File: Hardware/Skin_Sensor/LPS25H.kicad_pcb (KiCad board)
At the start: 2 copper layers, 55 x 55 mm, 49 parts, among them SW1 SW_PUSH, U1 ADP7102, U2 ATSAMD21E18A, U3 AVRISP, U4 LSM9DS1, U5 LP5521YQ, X1 ABS06

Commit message: Fixed pour issues
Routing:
- net GND: track 196.5 -> 200.9 mm, vias 12 -> 11
- net (no net): track 0.32 -> 0.37 mm, vias 0 -> 1
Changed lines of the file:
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@@
     (links 162)
     (no_connects 0)
-    (area 130.545445 70.825409 205.880001 129.245302)
+    (area 123.2 69.2 205.880001 130.350001)
     (thickness 1.6)
     (drawings 91)
@@
   (segment (start 159.172703 87.557501) (end 159.172703 87.840344) (width 0.25) (layer B.Cu) (net 0))
   (segment (start 159.137348 88.47674) (end 159.137348 88.512095) (width 0.25) (layer B.Cu) (net 0))
-  (segment (start 158.9984 104.9484) (end 159 104.95) (width 0.25) (layer F.Cu) (net 0))
+  (segment (start 153.05 102.5) (end 153.05 102.45) (width 0.2) (layer F.Cu) (net 0))
+  (via (at 153.05 102.45) (size 0.6) (drill 0.4) (layers F.Cu B.Cu) (net 0))
   (segment (start 165.75 103) (end 164.55 104.2) (width 0.5) (layer B.Cu) (net 1))
   (via (at 165.3 94.65) (size 0.6) (drill 0.4) (layers F.Cu B.Cu) (net 1))
@@
   (segment (start 158.394885 81.053514) (end 158.394885 85.05) (width 0.25) (layer F.Cu) (net 1))
   (segment (start 158.394885 85.05) (end 158.394885 85.082627) (width 0.25) (layer F.Cu) (net 1))
-  (segment (start 163.6 107.55) (end 163.55 107.6) (width 0.25) (layer B.Cu) (net 2))
+  (segment (start 160 109.15) (end 162.7 109.15) (width 0.25) (layer B.Cu) (net 2))
   (via (at 163.5 107.6) (size 0.6) (drill 0.4) (layers F.Cu B.Cu) (net 2))
-  (segment (start 163.55 107.6) (end 163.5 107.6) (width 0.25) (layer B.Cu) (net 2))
-  (segment (start 164.9 102.15) (end 165 102.05) (width 0.25) (layer F.Cu) (net 2) (status C00000))
-  (segment (start 165 102.05) (end 165 100.7) (width 0.25) (layer F.Cu) (net 2) (status 400000))
+  (segment (start 163.5 108.35) (end 163.5 107.6) (width 0.25) (layer B.Cu) (net 2))
+  (segment (start 162.7 109.15) (end 163.5 108.35) (width 0.25) (layer B.Cu) (net 2))
+  (segment (start 164.9 102.15) (end 165 102.05) (width 0.25) (layer F.Cu) (net 2))
+  (segment (start 165 102.05) (end 165 100.7) (width 0.25) (layer F.Cu) (net 2))
   (via (at 165 100.7) (size 0.6) (drill 0.4) (layers F.Cu B.Cu) (net 2))
-  (segment (start 165.4 101.425) (end 164.9 101.925) (width 0.25) (layer F.Cu) (net 2) (status C00000))
-  (segment (start 164.9 101.925) (end 164.9 102.15) (width 0.25) (layer F.Cu) (net 2) (status C00000))
+  (segment (start 165.4 101.425) (end 164.9 101.925) (width 0.25) (layer F.Cu) (net 2))
+  (segment (start 164.9 101.925) (end 164.9 102.15) (width 0.25) (layer F.Cu) (net 2))
   (segment (start 164.175 104.375) (end 164.075 104.375) (width 0.25) (layer F.Cu) (net 2))
   (via (at 163 103.2) (size 0.6) (drill 0.4) (layers F.Cu B.Cu) (net 2))
   (segment (start 163 103.3) (end 163 103.2) (width 0.25) (layer F.Cu) (net 2))
   (segment (start 164.075 104.375) (end 163 103.3) (width 0.25) (layer F.Cu) (net 2))
-  (via (at 159.4 100.65) (size 0.6) (drill 0.4) (layers F.Cu B.Cu) (net 2) (status 800000))
-  (segment (start 159.4 100.65) (end 160 100.05) (width 0.2) (layer F.Cu) (net 2) (status C00000))
-  (segment (start 160 100.05) (end 160 100) (width 0.2) (layer F.Cu) (net 2) (status C00000))
-  (segment (start 153.05 102.5) (end 153.05 102.45) (width 0.2) (layer F.Cu) (net 2))
-  (via (at 153.05 102.45) (size 0.6) (drill 0.4) (layers F.Cu B.Cu) (net 2))
+  (via (at 159.4 100.65) (size 0.6) (drill 0.4) (layers F.Cu B.Cu) (net 2))
+  (segment (start 159.4 100.65) (end 160 100.05) (width 0.2) (layer F.Cu) (net 2))
+  (segment (start 160 100.05) (end 160 100) (width 0.2) (layer F.Cu) (net 2))
   (segment (start 162.04 109.25) (end 160.1 109.25) (width 0.2) (layer F.Cu) (net 2))
   (via (at 160 109.15) (size 0.6) (drill 0.4) (layers F.Cu B.Cu) (net 2))
@@
   (segment (start 162.8 102.55) (end 163.25 102.55) (width 0.25) (layer F.Cu) (net 3))
   (segment (start 163.25 102.55) (end 163.65 102.95) (width 0.25) (layer F.Cu) (net 3))
-  (segment (start 162.35 103.6) (end 162 103.95) (width 0.25) (layer F.Cu) (net 3) (status 800000))
+  (segment (start 162.35 103.6) (end 162 103.95) (width 0.25) (layer F.Cu) (net 3))
   (segment (start 163.65 103.35) (end 163.65 102.95) (width 0.25) (layer F.Cu) (net 3))
   (segment (start 164.2 103.9) (end 163.65 103.35) (width 0.25) (layer F.Cu) (net 3))
   (segment (start 163.4 106.7) (end 163.4 104.3) (width 0.25) (layer F.Cu) (net 3))
   (segment (start 163.4 104.3) (end 163.05 103.95) (width 0.25) (layer F.Cu) (net 3))
-  (segment (start 163.05 103.95) (end 162 103.95) (width 0.25) (layer F.Cu) (net 3) (status 800000))
+  (segment (start 163.05 103.95) (end 162 103.95) (width 0.25) (layer F.Cu) (net 3))
   (segment (start 162.9 107.4) (end 162.9 107.95) (width 0.25) (layer F.Cu) (net 3))
   (segment (start 163.4 106.7) (end 162.9 107.2) (width 0.25) (layer F.Cu) (net 3))
@@
   (via (at 164.1 102.5) (size 0.6) (drill 0.4) (layers F.Cu B.Cu) (net 41))
   (segment (start 166 101.7) (end 165.2 102.5) (width 0.2) (layer B.Cu) (net 41))
-  (segment (start 164.25 103.25) (end 164.9 103.25) (width 0.25) (layer F.Cu) (net 41) (status 800000))
+  (segment (start 164.25 103.25) (end 164.9 103.25) (width 0.25) (layer F.Cu) (net 41))
   (segment (start 164.1 103.1) (end 164.25 103.25) (width 0.25) (layer F.Cu) (net 41))
   (segment (start 168.215 98.725) (end 168.215 99) (width 0.2) (layer F.Cu) (net 41))

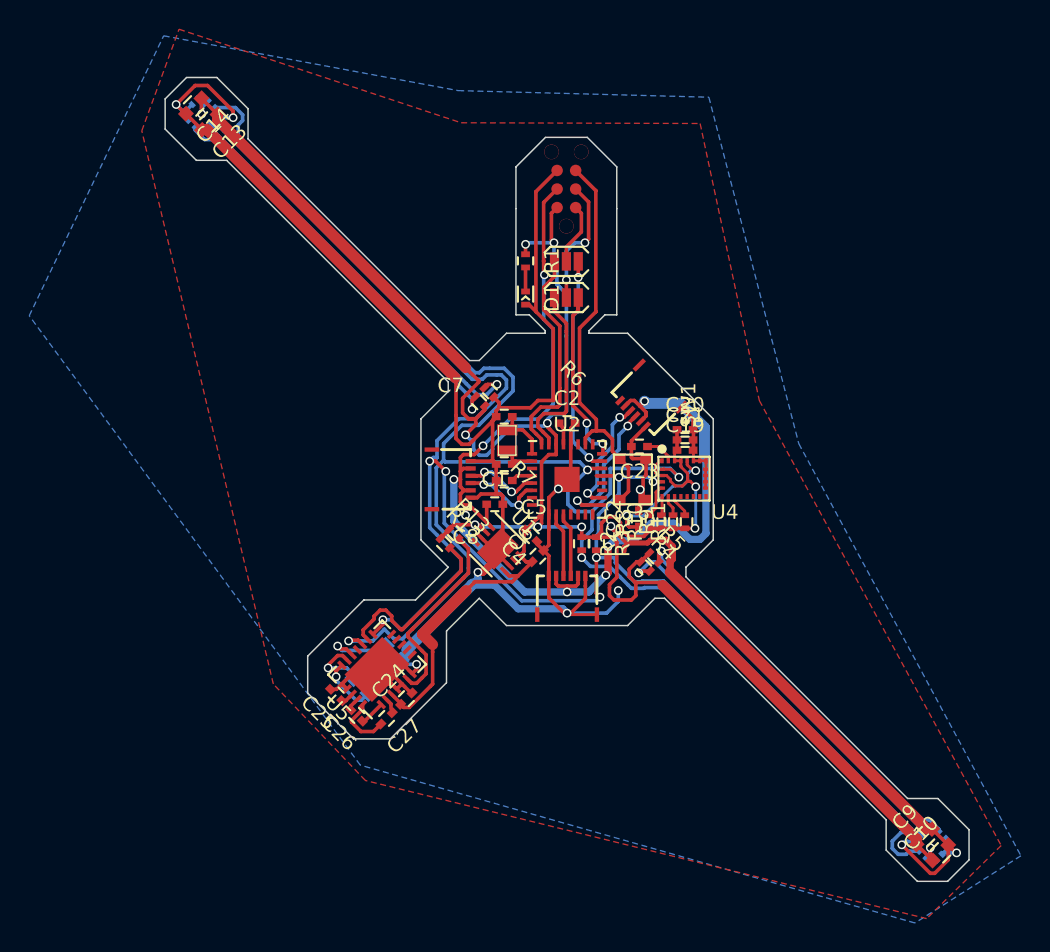
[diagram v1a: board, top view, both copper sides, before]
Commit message: Added sensor and cleaned up the board
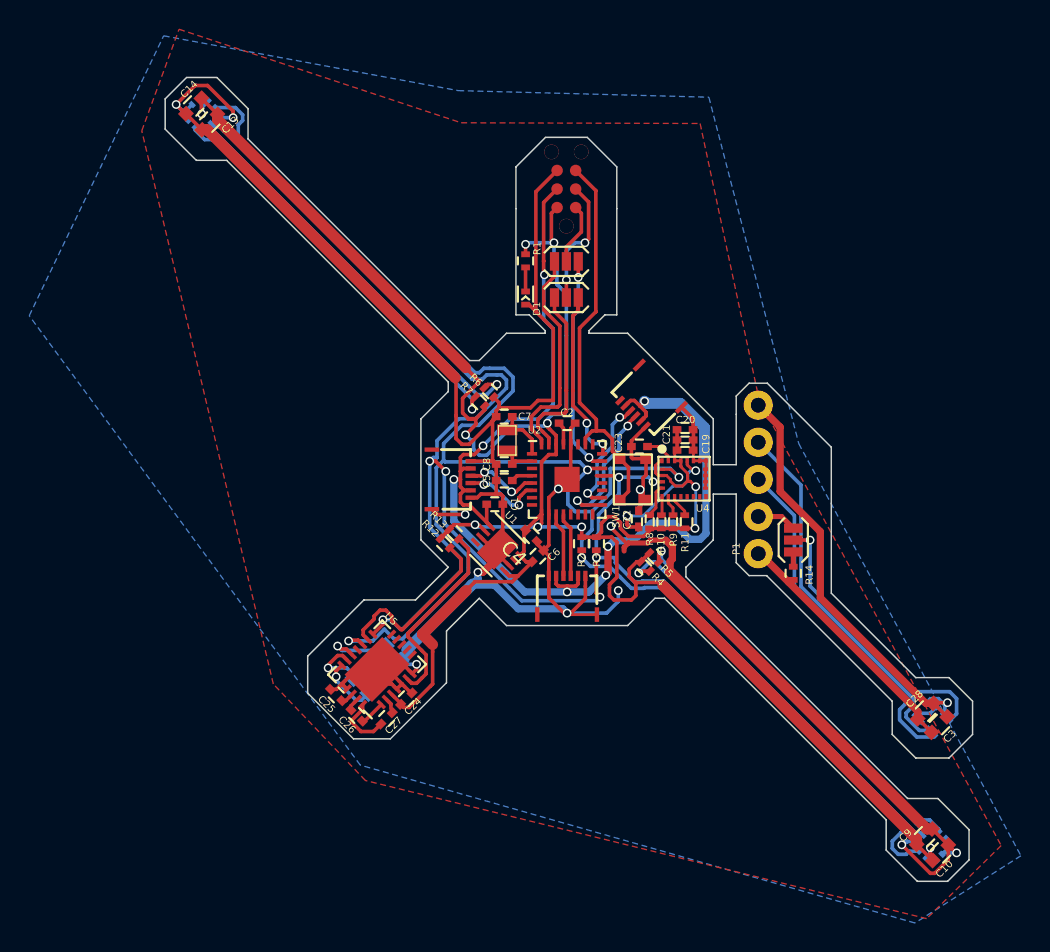
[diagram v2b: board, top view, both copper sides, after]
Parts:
- added C15: sj2, _Fab_Footprint:SJ-2-1-no, F.Cu at (175.5, 104.2)
- added C28: 100nF, Capacitors_SMD:C_0603, F.Cu at (184.5, 115.8)
- added C3: 100nF, Capacitors_SMD:C_0603, F.Cu at (185.5, 116.8)
- added P1: CONN_01X05, _Fab_Footprint:2.54mmX05, F.Cu at (173.1, 100.0)
- added R14: 100k, Resistors_SMD:R_0402, F.Cu at (175.5, 106.4)
- added U6: DPS310, _CSL:8-LGA, B.Cu at (185.0, 116.3)
- C19: value 100nF -> 10uF
- C22: value 100nF -> 10nF
- C24, C25: value 4.7UF -> 1uF
- C26, C27: value 4.7UF -> 0.47uF
- R1: value 10k -> 330
- R10, R11, R12, R13, R4, R5, R6, R7, R8, R9: value RES -> 10k
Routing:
- net VDD_EX: track 0.00 -> 30.1 mm, vias 0 -> 1
- net SDA_EX: track 0.00 -> 25.4 mm
- net SCL_EX: track 0.00 -> 23.8 mm
- net GND_EX: track 0.00 -> 19.3 mm
- net Net-(C15-Pad1): track 0.00 -> 19.2 mm, vias 0 -> 1
- net INT_EX: track 0.00 -> 2.73 mm
- net GND: track 200.9 -> 203.3 mm, vias 11 -> 12
- net Net-(C15-Pad3): track 0.00 -> 1.01 mm
- net (no net): track 0.37 -> 0.32 mm, vias 1 -> 0
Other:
- board size 55 x 55 mm -> 55.2 x 55 mm
